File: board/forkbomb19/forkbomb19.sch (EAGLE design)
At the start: 52 parts, among them SW1 SPST_TACT-KMR2, U1 ESP-WROOM-03, X2 22-23-2021, X3 POT_GND, X4 POT_3V3, X5 POT_SIG

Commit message: silkscreen placement
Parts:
- renumbered JP1 to HRDRST, JP2 to ADDR, LED1 to TX, LED2 to RX, X2 to BATT
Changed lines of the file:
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@@
 <part name="U1" library="forkbomb19" deviceset="ESP-WROOM-03" device=""/>
 <part name="U2" library="forkbomb19" deviceset="MICROBUILDER_AMG8833" device=""/>
-<part name="JP1" library="SparkFun-Jumpers" library_urn="urn:adsk.eagle:library:528" deviceset="JUMPER-SMT_2_NO" device="_SILK_ROUND" package3d_urn="urn:adsk.eagle:package:39280/1" value=""/>
+<part name="HRDRST" library="SparkFun-Jumpers" library_urn="urn:adsk.eagle:library:528" deviceset="JUMPER-SMT_2_NO" device="_SILK_ROUND" package3d_urn="urn:adsk.eagle:package:39280/1" value=""/>
 <part name="R1" library="resistor" library_urn="urn:adsk.eagle:library:348" deviceset="R-US_" device="R0603" package3d_urn="urn:adsk.eagle:package:23555/2"/>
 <part name="C1" library="resistor" library_urn="urn:adsk.eagle:library:348" deviceset="C-US" device="C0603" package3d_urn="urn:adsk.eagle:package:23616/2" value="100nF"/>
@@
 <part name="C12" library="resistor" library_urn="urn:adsk.eagle:library:348" deviceset="CPOL-US" device="153CLV-0405" package3d_urn="urn:adsk.eagle:package:23397/1" value="10uF"/>
 <part name="GND17" library="supply1" deviceset="GND" device=""/>
-<part name="X2" library="con-molex" library_urn="urn:adsk.eagle:library:165" deviceset="22-23-2021" device="" package3d_urn="urn:adsk.eagle:package:8078633/1"/>
+<part name="BATT" library="con-molex" library_urn="urn:adsk.eagle:library:165" deviceset="22-23-2021" device="" package3d_urn="urn:adsk.eagle:package:8078633/1"/>
 <part name="X3" library="con-samtec" library_urn="urn:adsk.eagle:library:184" deviceset="TSW-101-*-G-S" device="" technology="07" value="POT_GND"/>
 <part name="X4" library="con-samtec" library_urn="urn:adsk.eagle:library:184" deviceset="TSW-101-*-G-S" device="" technology="07" value="POT_3V3"/>
 <part name="X5" library="con-samtec" library_urn="urn:adsk.eagle:library:184" deviceset="TSW-101-*-G-S" device="" technology="07" value="POT_SIG"/>
 <part name="SW1" library="adafruit" library_urn="urn:adsk.eagle:library:420" deviceset="SPST_TACT" device="-KMR2" package3d_urn="urn:adsk.eagle:package:6240885/1"/>
-<part name="LED1" library="led" library_urn="urn:adsk.eagle:library:259" deviceset="LED" device="SML0603" package3d_urn="urn:adsk.eagle:package:15832/1"/>
-<part name="LED2" library="led" library_urn="urn:adsk.eagle:library:259" deviceset="LED" device="SML0603" package3d_urn="urn:adsk.eagle:package:15832/1"/>
+<part name="TX" library="led" library_urn="urn:adsk.eagle:library:259" deviceset="LED" device="SML0603" package3d_urn="urn:adsk.eagle:package:15832/1"/>
+<part name="RX" library="led" library_urn="urn:adsk.eagle:library:259" deviceset="LED" device="SML0603" package3d_urn="urn:adsk.eagle:package:15832/1"/>
 <part name="R2" library="resistor" library_urn="urn:adsk.eagle:library:348" deviceset="R-US_" device="R0603" package3d_urn="urn:adsk.eagle:package:23555/2" value="300"/>
 <part name="R12" library="resistor" library_urn="urn:adsk.eagle:library:348" deviceset="R-US_" device="R0603" package3d_urn="urn:adsk.eagle:package:23555/2" value="300"/>
 <part name="+3V12" library="supply1" library_urn="urn:adsk.eagle:library:371" deviceset="+3V3" device=""/>
-<part name="JP2" library="SparkFun-Jumpers" library_urn="urn:adsk.eagle:library:528" deviceset="JUMPER-SMT_2_NO" device="_SILK_ROUND" package3d_urn="urn:adsk.eagle:package:39280/1" value=""/>
+<part name="ADDR" library="SparkFun-Jumpers" library_urn="urn:adsk.eagle:library:528" deviceset="JUMPER-SMT_2_NO" device="_SILK_ROUND" package3d_urn="urn:adsk.eagle:package:39280/1" value=""/>
 <part name="GND18" library="supply1" library_urn="urn:adsk.eagle:library:371" deviceset="GND" device=""/>
 </parts>
@@
 <attribute name="VALUE" x="111.76" y="-35.56" size="1.778" layer="96"/>
 </instance>
-<instance part="JP1" gate="G$1" x="-35.56" y="30.48" smashed="yes">
+<instance part="HRDRST" gate="G$1" x="-35.56" y="30.48" smashed="yes">
 <attribute name="NAME" x="-38.1" y="33.02" size="1.778" layer="95" font="vector"/>
 <attribute name="VALUE" x="-38.1" y="27.94" size="1.778" layer="96" font="vector" align="top-left"/>
@@
 <attribute name="VALUE" x="-111.76" y="12.7" size="1.778" layer="96" rot="MR0"/>
 </instance>
-<instance part="X2" gate="-1" x="-215.9" y="5.08" smashed="yes">
+<instance part="BATT" gate="-1" x="-215.9" y="5.08" smashed="yes">
 <attribute name="NAME" x="-213.36" y="4.318" size="1.524" layer="95"/>
 <attribute name="VALUE" x="-216.662" y="6.477" size="1.778" layer="96"/>
 </instance>
-<instance part="X2" gate="-2" x="-215.9" y="2.54" smashed="yes">
+<instance part="BATT" gate="-2" x="-215.9" y="2.54" smashed="yes">
 <attribute name="NAME" x="-213.36" y="1.778" size="1.524" layer="95"/>
 </instance>
@@
 <attribute name="VALUE" x="46.355" y="-21.59" size="1.778" layer="96"/>
 </instance>
-<instance part="LED1" gate="G$1" x="149.86" y="63.5" smashed="yes" rot="R270">
+<instance part="TX" gate="G$1" x="149.86" y="63.5" smashed="yes" rot="R270">
 <attribute name="NAME" x="145.288" y="59.944" size="1.778" layer="95"/>
 <attribute name="VALUE" x="145.288" y="57.785" size="1.778" layer="96"/>
 </instance>
-<instance part="LED2" gate="G$1" x="149.86" y="55.88" smashed="yes" rot="R270">
+<instance part="RX" gate="G$1" x="149.86" y="55.88" smashed="yes" rot="R270">
 <attribute name="NAME" x="145.288" y="52.324" size="1.778" layer="95"/>
 <attribute name="VALUE" x="145.288" y="50.165" size="1.778" layer="96"/>
@@
 <attribute name="VALUE" x="170.18" y="63.5" size="1.778" layer="96" rot="R90"/>
 </instance>
-<instance part="JP2" gate="G$1" x="86.36" y="-30.48" smashed="yes" rot="R90">
+<instance part="ADDR" gate="G$1" x="86.36" y="-30.48" smashed="yes" rot="R90">
 <attribute name="NAME" x="83.82" y="-33.02" size="1.778" layer="95" font="vector" rot="R90"/>
 <attribute name="VALUE" x="88.9" y="-33.02" size="1.778" layer="96" font="vector" rot="R90" align="top-left"/>
@@
 <pinref part="R1" gate="G$1" pin="1"/>
 <wire x1="-17.78" y1="30.48" x2="-25.4" y2="30.48" width="0.1524" layer="91"/>
-<pinref part="JP1" gate="G$1" pin="2"/>
+<pinref part="HRDRST" gate="G$1" pin="2"/>
 <wire x1="-25.4" y1="30.48" x2="-30.48" y2="30.48" width="0.1524" layer="91"/>
 <junction x="-25.4" y="30.48"/>
@@
 <segment>
 <pinref part="GND2" gate="1" pin="GND"/>
-<pinref part="JP1" gate="G$1" pin="1"/>
+<pinref part="HRDRST" gate="G$1" pin="1"/>
 <wire x1="-43.18" y1="27.94" x2="-43.18" y2="30.48" width="0.1524" layer="91"/>
 <wire x1="-43.18" y1="30.48" x2="-40.64" y2="30.48" width="0.1524" layer="91"/>
@@
 <pinref part="GND23" gate="1" pin="GND"/>
 <wire x1="-218.44" y1="2.54" x2="-226.06" y2="2.54" width="0.1524" layer="91"/>
-<pinref part="X2" gate="-2" pin="S"/>
+<pinref part="BATT" gate="-2" pin="S"/>
 </segment>
 <segment>
@@
 </segment>
 <segment>
-<pinref part="JP2" gate="G$1" pin="1"/>
+<pinref part="ADDR" gate="G$1" pin="1"/>
 <pinref part="GND18" gate="1" pin="GND"/>
 <wire x1="86.36" y1="-35.56" x2="86.36" y2="-38.1" width="0.1524" layer="91"/>
@@
 <wire x1="86.36" y1="-22.86" x2="86.36" y2="-25.4" width="0.1524" layer="91"/>
 <junction x="86.36" y="-22.86"/>
-<pinref part="JP2" gate="G$1" pin="2"/>
+<pinref part="ADDR" gate="G$1" pin="2"/>
 </segment>
 </net>
@@
 <wire x1="-226.06" y1="30.48" x2="-226.06" y2="5.08" width="0.1524" layer="91"/>
 <wire x1="-218.44" y1="5.08" x2="-226.06" y2="5.08" width="0.1524" layer="91"/>
-<pinref part="X2" gate="-1" pin="S"/>
+<pinref part="BATT" gate="-1" pin="S"/>
 </segment>
 </net>
@@
 <pinref part="U3" gate="G$1" pin="GPIO1/RXLED"/>
 <wire x1="139.7" y1="58.42" x2="144.78" y2="58.42" width="0.1524" layer="91"/>
-<pinref part="LED2" gate="G$1" pin="C"/>
+<pinref part="RX" gate="G$1" pin="C"/>
 <wire x1="144.78" y1="58.42" x2="144.78" y2="55.88" width="0.1524" layer="91"/>
 </segment>
@@
 <pinref part="U3" gate="G$1" pin="GPIO0/TXLED"/>
 <wire x1="139.7" y1="60.96" x2="144.78" y2="60.96" width="0.1524" layer="91"/>
-<pinref part="LED1" gate="G$1" pin="C"/>
+<pinref part="TX" gate="G$1" pin="C"/>
 <wire x1="144.78" y1="60.96" x2="144.78" y2="63.5" width="0.1524" layer="91"/>
 </segment>
@@
 <segment>
 <pinref part="R2" gate="G$1" pin="2"/>
-<pinref part="LED1" gate="G$1" pin="A"/>
+<pinref part="TX" gate="G$1" pin="A"/>
 <wire x1="154.94" y1="63.5" x2="152.4" y2="63.5" width="0.1524" layer="91"/>
 </segment>
@@
 <segment>
 <pinref part="R12" gate="G$1" pin="2"/>
-<pinref part="LED2" gate="G$1" pin="A"/>
+<pinref part="RX" gate="G$1" pin="A"/>
 <wire x1="154.94" y1="55.88" x2="152.4" y2="55.88" width="0.1524" layer="91"/>
 </segment>

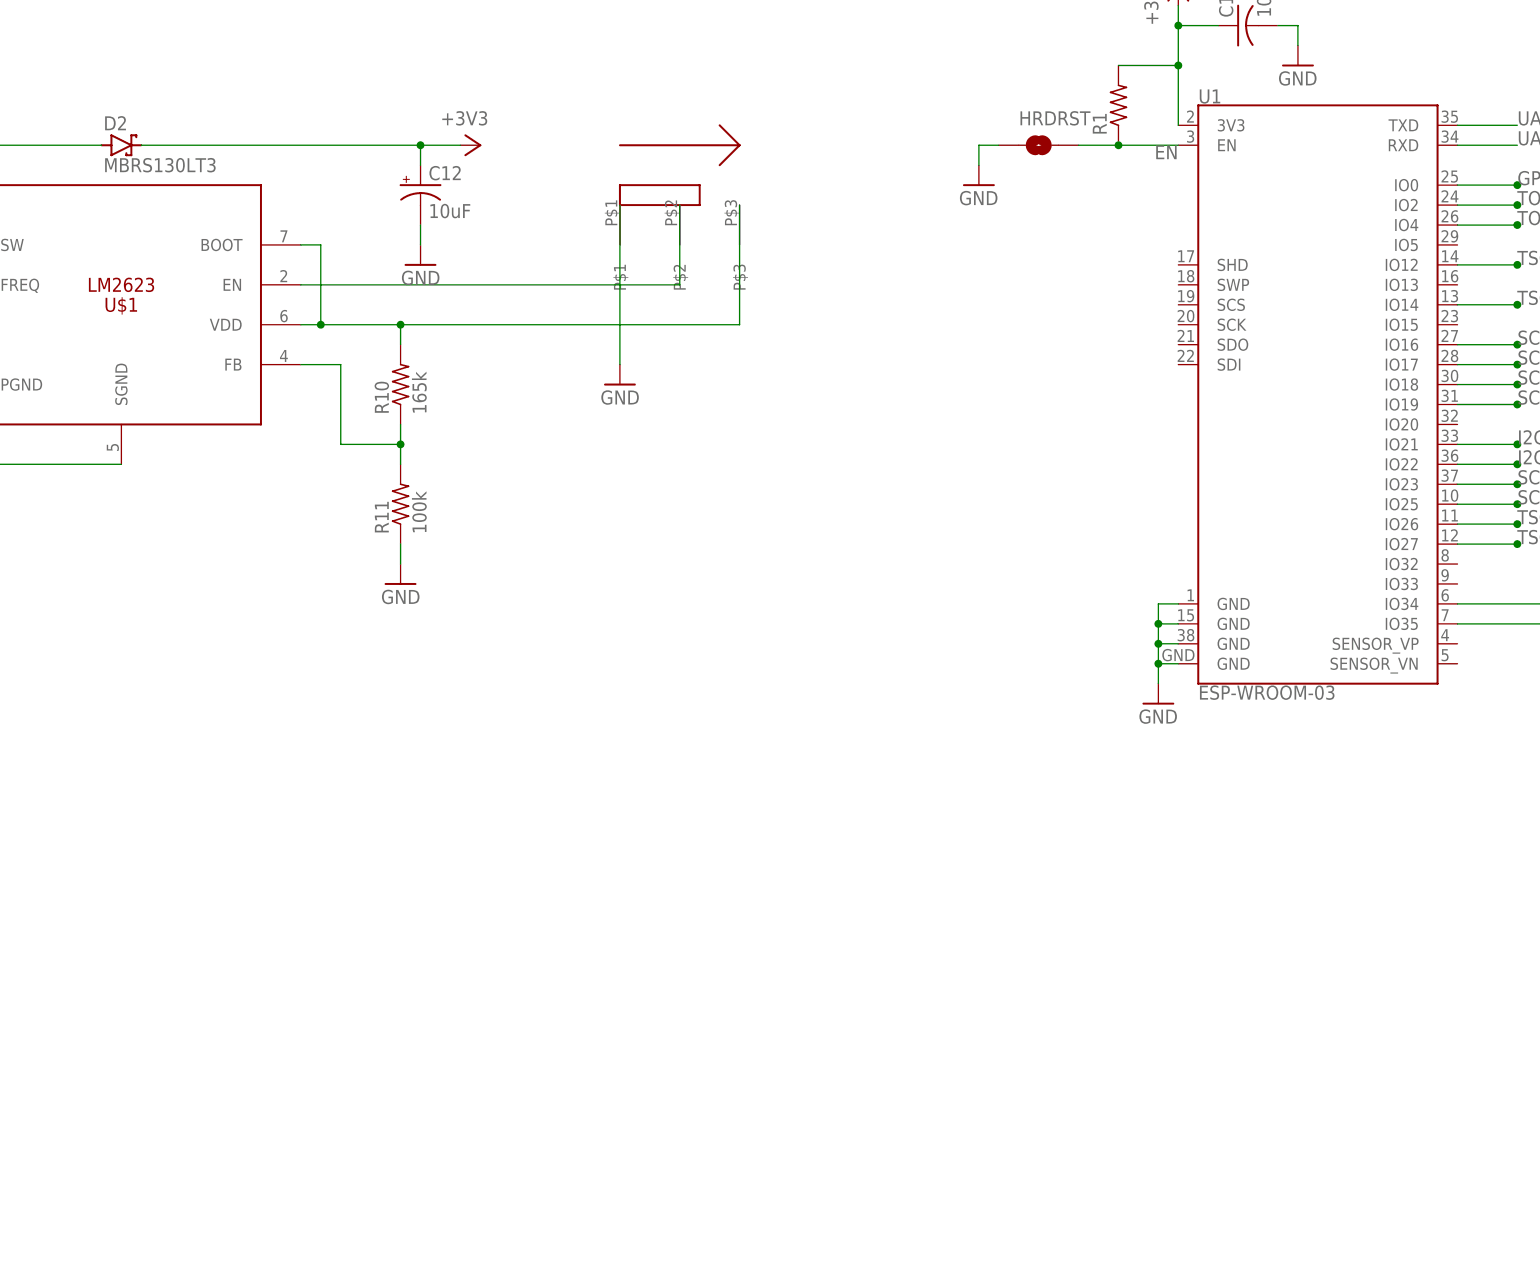
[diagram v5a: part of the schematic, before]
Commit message: created screen
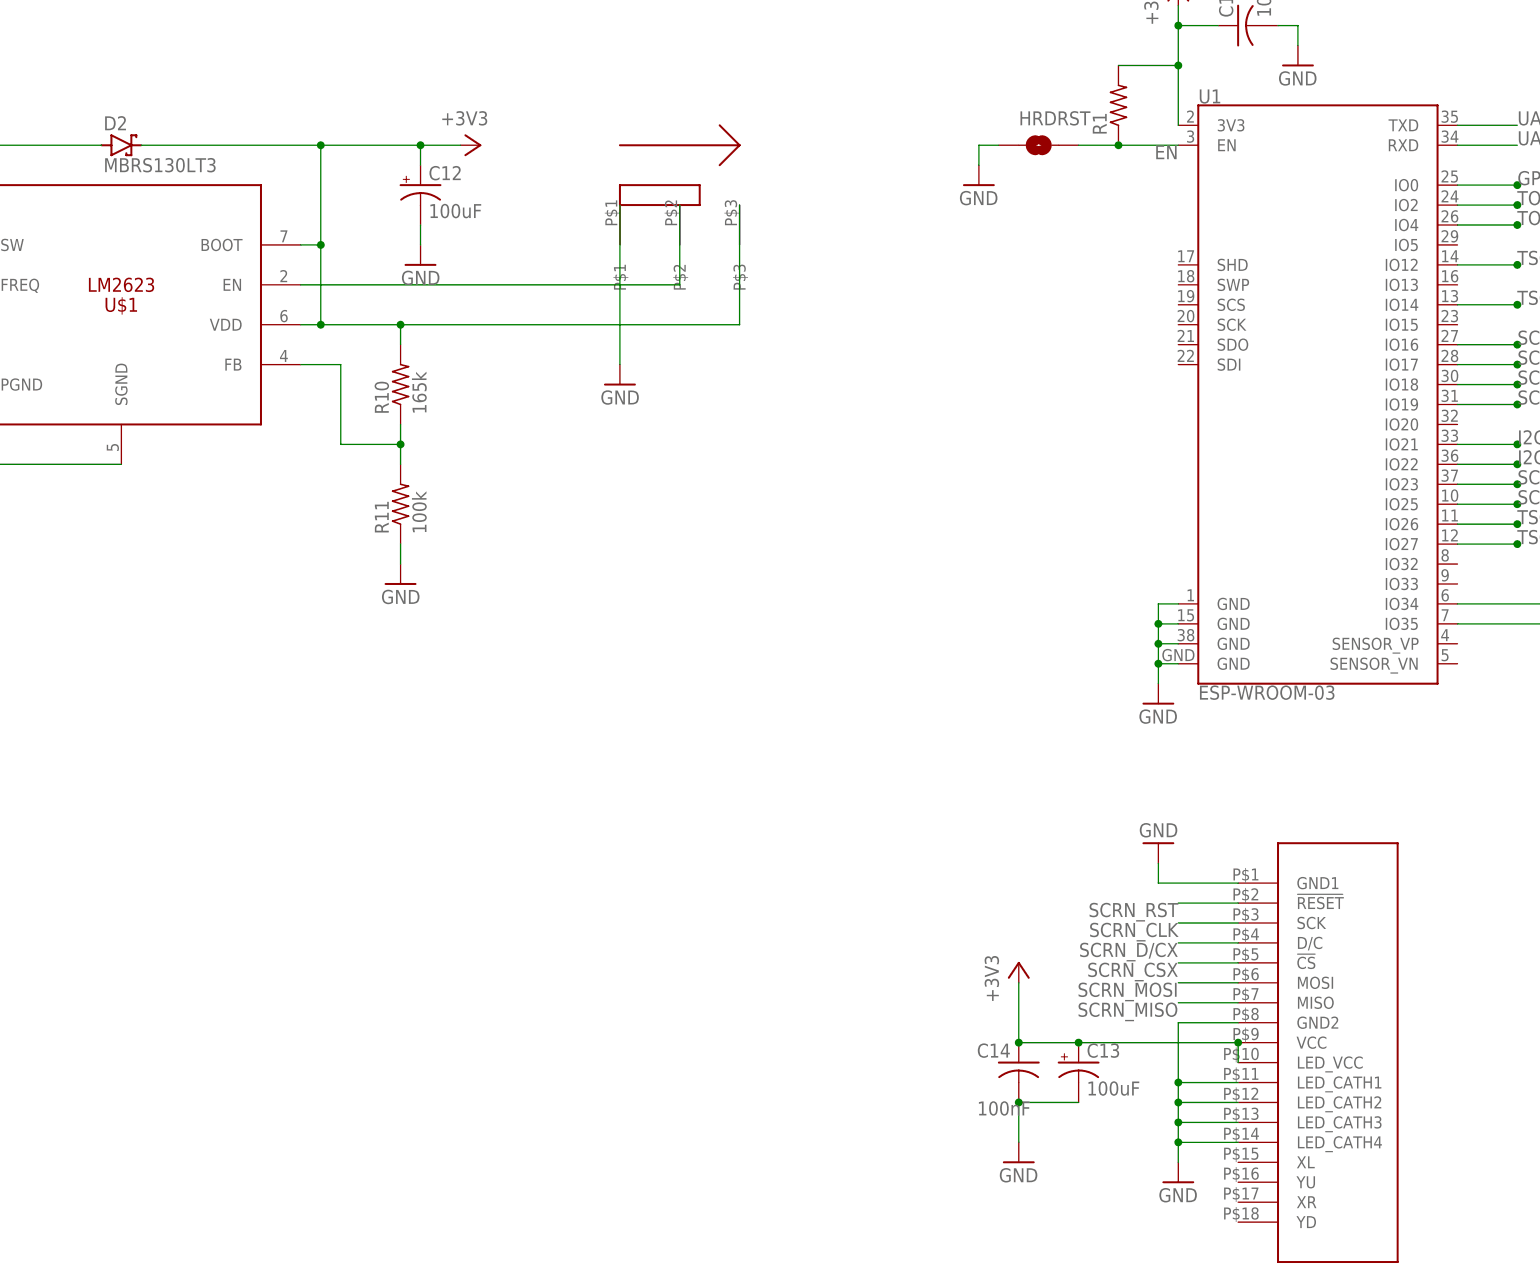
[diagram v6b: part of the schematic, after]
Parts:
- added C13: 100uF, resistor:CPOL-USC/6032-28R
- added C14: 100nF, resistor:C-USC0603
- added U$2: SPI_TFT, forkbomb19:SPI_TFT
- C10: device resistor:CPOL-US153CLV-0405 -> resistor:CPOL-USB/3528-21R
- C12: value 10uF -> 100uF; device resistor:CPOL-US153CLV-0405 -> resistor:CPOL-USC/6032-28R
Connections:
- removed net N$16: R10.2, U$1.BOOT, U$1.VDD, U$17.P$3
- net +3V3: now also C13.+, C14.1, R10.2, U$1.BOOT, U$1.VDD, U$17.P$3, U$2.LED_VCC, U$2.VCC
- net GND: now also C13.-, C14.2, U$2.GND1, U$2.GND2, U$2.LED_CATH1, U$2.LED_CATH2, U$2.LED_CATH3, U$2.LED_CATH4
- net SCRN_CLK: now also U$2.SCK
- net SCRN_CSX: now also U$2.!CS
- net SCRN_D/CX: now also U$2.D/C
- net SCRN_MISO: now also U$2.MISO
- net SCRN_MOSI: now also U$2.MOSI
- net SCRN_RST: now also U$2.!RESET

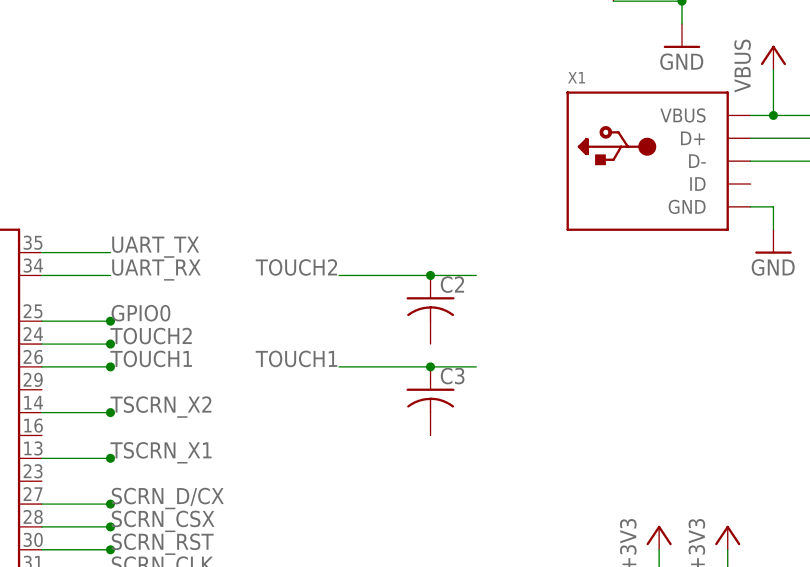
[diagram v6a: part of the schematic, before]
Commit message: added touch pad
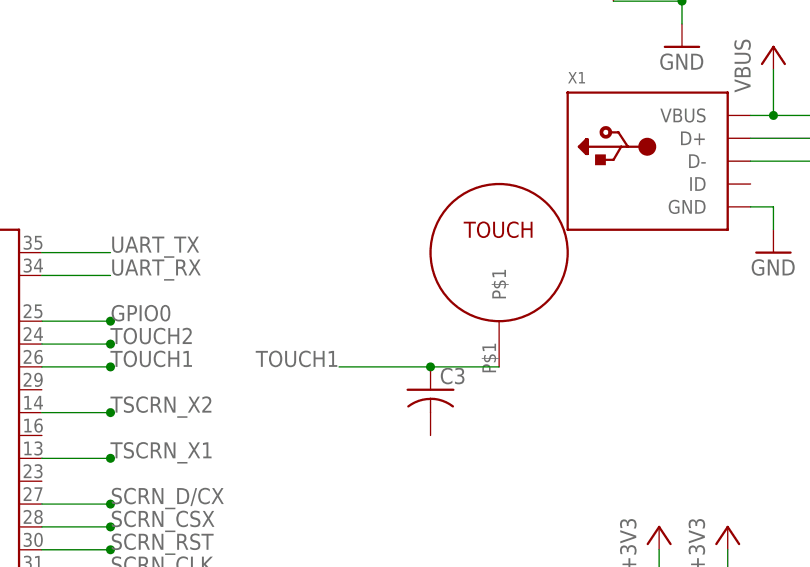
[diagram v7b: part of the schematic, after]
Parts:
- removed C2: (no value), resistor:C-USC0805
- added TOUCH: TOUCHPAD, forkbomb19:TOUCHPAD
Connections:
- net TOUCH1: now also TOUCH.P$1
- net TOUCH2: no longer C2.1
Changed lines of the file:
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@@
 <part name="GND5" library="supply1" library_urn="urn:adsk.eagle:library:371" deviceset="GND" device=""/>
 <part name="+3V2" library="supply1" library_urn="urn:adsk.eagle:library:371" deviceset="+3V3" device=""/>
-<part name="C2" library="resistor" library_urn="urn:adsk.eagle:library:348" deviceset="C-US" device="C0805" package3d_urn="urn:adsk.eagle:package:23617/2"/>
 <part name="C3" library="resistor" library_urn="urn:adsk.eagle:library:348" deviceset="C-US" device="C0805" package3d_urn="urn:adsk.eagle:package:23617/2"/>
 <part name="+3V3" library="supply1" library_urn="urn:adsk.eagle:library:371" deviceset="+3V3" device=""/>
@@
 <part name="GND21" library="supply1" library_urn="urn:adsk.eagle:library:371" deviceset="GND" device=""/>
 <part name="+3V13" library="supply1" library_urn="urn:adsk.eagle:library:371" deviceset="+3V3" device=""/>
+<part name="TOUCH" library="forkbomb19" deviceset="TOUCHPAD" device=""/>
 </parts>
 <sheets>
@@
 <attribute name="VALUE" x="63.5" y="-30.48" size="1.778" layer="96" rot="R90"/>
 </instance>
-<instance part="C2" gate="G$1" x="60.96" y="27.94" smashed="yes">
-<attribute name="NAME" x="61.976" y="28.575" size="1.778" layer="95"/>
-<attribute name="VALUE" x="61.976" y="23.749" size="1.778" layer="96"/>
-</instance>
 <instance part="C3" gate="G$1" x="60.96" y="17.78" smashed="yes">
 <attribute name="NAME" x="61.976" y="18.415" size="1.778" layer="95"/>
@@
 <instance part="+3V13" gate="G$1" x="-38.1" y="-73.66" smashed="yes">
 <attribute name="VALUE" x="-40.64" y="-78.74" size="1.778" layer="96" rot="R90"/>
+</instance>
+<instance part="TOUCH" gate="G$1" x="68.58" y="33.02" smashed="yes">
+<attribute name="NAME" x="68.58" y="35.56" size="1.778" layer="94" align="center"/>
 </instance>
 </instances>
@@
 <wire x1="50.8" y1="20.32" x2="60.96" y2="20.32" width="0.1524" layer="91"/>
 <pinref part="C3" gate="G$1" pin="1"/>
-<wire x1="60.96" y1="20.32" x2="66.04" y2="20.32" width="0.1524" layer="91"/>
+<wire x1="60.96" y1="20.32" x2="68.58" y2="20.32" width="0.1524" layer="91"/>
 <junction x="60.96" y="20.32"/>
 <label x="50.8" y="20.32" size="1.778" layer="95" rot="MR0"/>
+<pinref part="TOUCH" gate="G$1" pin="P$1"/>
 </segment>
 </net>
@@
 <label x="25.4" y="22.86" size="1.778" layer="95"/>
 </segment>
-<segment>
-<wire x1="50.8" y1="30.48" x2="60.96" y2="30.48" width="0.1524" layer="91"/>
-<pinref part="C2" gate="G$1" pin="1"/>
-<wire x1="60.96" y1="30.48" x2="66.04" y2="30.48" width="0.1524" layer="91"/>
-<junction x="60.96" y="30.48"/>
-<label x="50.8" y="30.48" size="1.778" layer="95" rot="MR0"/>
-</segment>
-</net>
+</net>
